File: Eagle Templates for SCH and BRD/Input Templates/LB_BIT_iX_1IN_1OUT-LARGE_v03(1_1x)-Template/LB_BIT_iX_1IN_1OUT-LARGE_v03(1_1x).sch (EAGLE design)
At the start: 16 parts, among them U1 LV321SOT23-5, U2 LV321SOT23-5

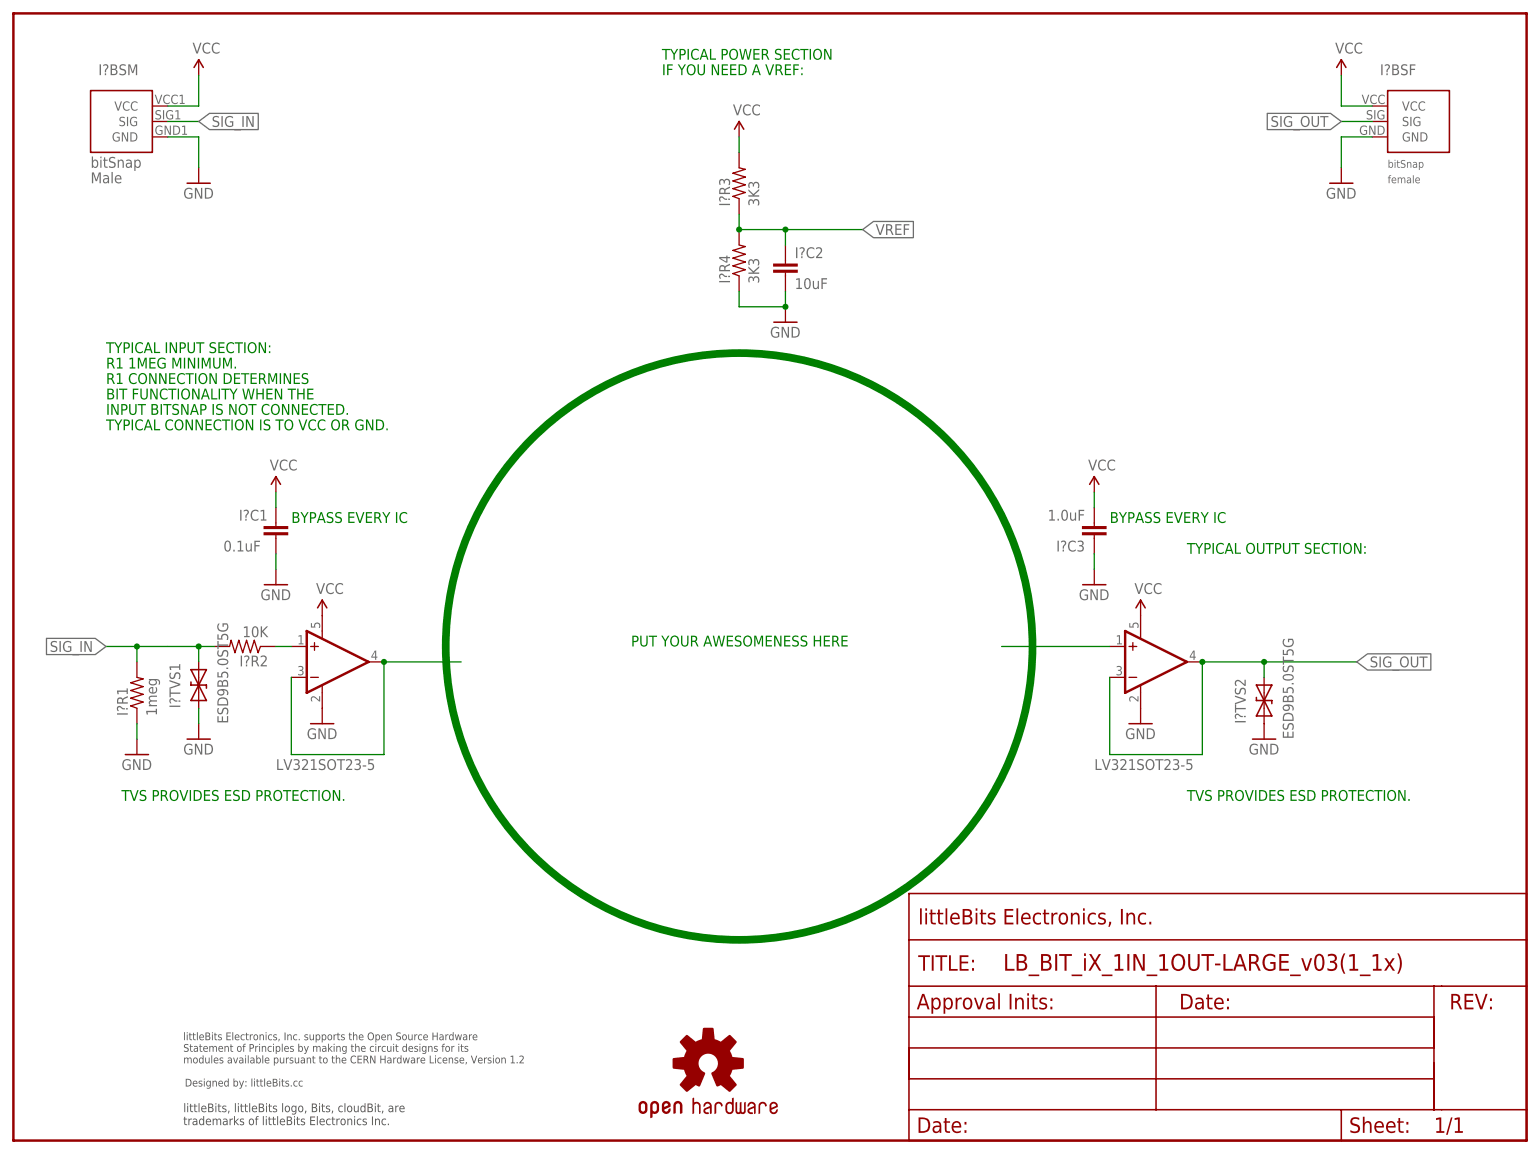
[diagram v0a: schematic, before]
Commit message: Updated templates
- Added ferrite beads
- Moved text and annotations off of Nets layer
- Minor layout changes
- Removed I/O/W prefix from reference designators
- Removed output stage components from output bits
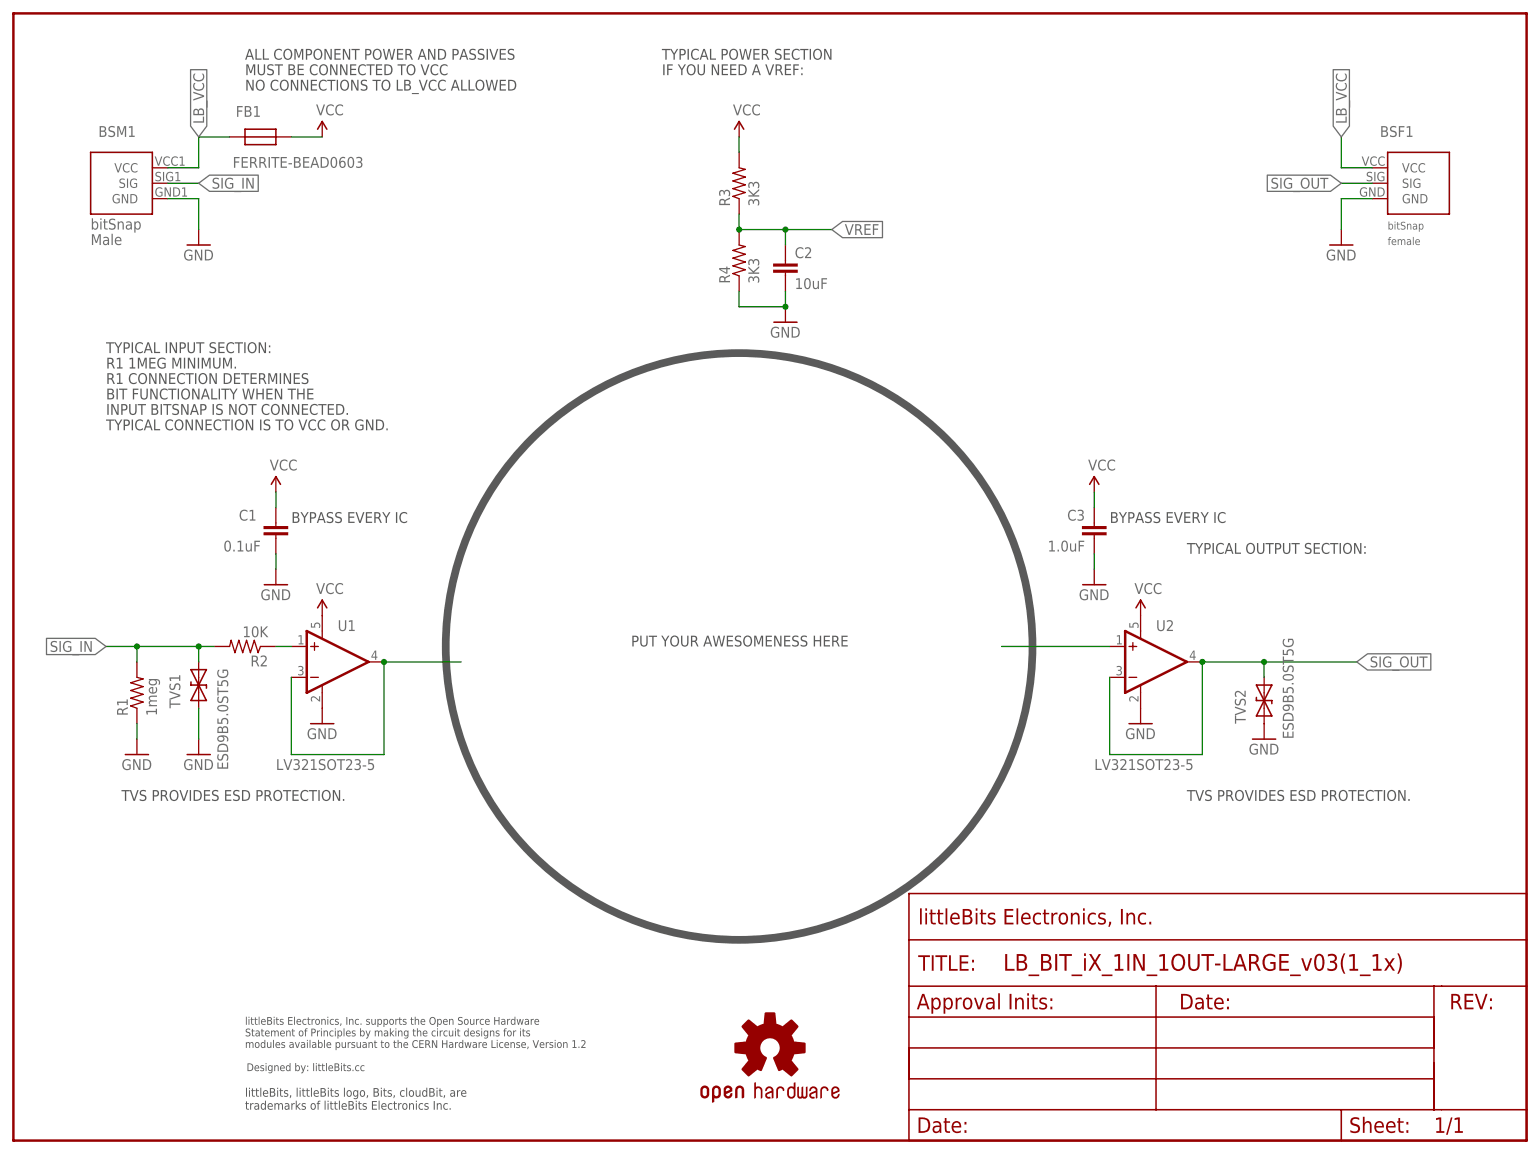
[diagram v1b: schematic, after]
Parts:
- removed I?BSF: BITSNAP_V03_FEMALE, bitSnap:BITSNAP_V03_FEMALE
- removed I?BSM: BITSNAP_V03_MALE, bitSnap:BITSNAP_V03_MALE
- removed U$4: OSHW-LOGOL, LITTLEBITS131206:OSHW-LOGOL
- added BSF1: BITSNAP_V03_FEMALE, bitSnap:BITSNAP_V03_FEMALE
- added BSM1: BITSNAP_V03_MALE, bitSnap:BITSNAP_V03_MALE
- added FB1: FERRITE-BEAD0603, LITTLEBITS:FERRITE-BEAD0603
- added U$2: OSHWCREDIT, LITTLEBITS:OSHWCREDIT
- U$1: value OSHWCREDIT -> OSHW-LOGOL; device LITTLEBITS:OSHWCREDIT -> LITTLEBITS131206:OSHW-LOGOL
- renumbered FRAME1 to U$3, I?C1 to C1, I?C2 to C2, I?C3 to C3, I?R1 to R1, I?R2 to R2, I?R3 to R3, I?R4 to R4, I?TVS1 to TVS1, I?TVS2 to TVS2
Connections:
- new net LB_VCC: BSF1.VCC, BSM1.VCC, FB1.P$2
- net GND: now also BSF1.GND, BSM1.GND; no longer I?BSF.GND, I?BSM.GND
- net SIG_IN: now also BSM1.SIG; no longer I?BSM.SIG
- net SIG_OUT: now also BSF1.SIG; no longer I?BSF.SIG
- net VCC: now also FB1.P$1; no longer I?BSF.VCC, I?BSM.VCC
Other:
- note added: "ALL COMPONENT POWER AND PASSIVES"
- note added: "MUST BE CONNECTED TO VCC"
- note added: "NO CONNECTIONS TO LB_VCC ALLOWED"
